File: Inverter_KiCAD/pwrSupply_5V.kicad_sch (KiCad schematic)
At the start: 2 parts, among them U11 17791063215

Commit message: add break
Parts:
- R21: footprint (none) -> Resistor_SMD:R_0603_1608Metric_Pad0.98x0.95mm_HandSolder
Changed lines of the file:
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@@
       (effects (font (size 1.27 1.27)) (justify left))
     )
-    (property "Footprint" "" (at 64.77 34.29 0)
+    (property "Footprint" "Resistor_SMD:R_0603_1608Metric_Pad0.98x0.95mm_HandSolder" (at 64.77 34.29 0)
       (effects (font (size 1.27 1.27)) hide)
     )

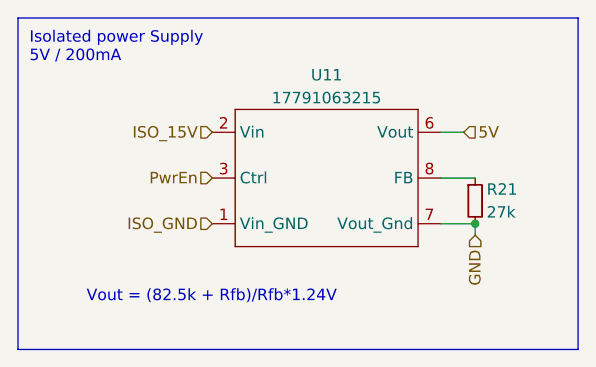
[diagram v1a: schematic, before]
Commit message: clear schematic errors
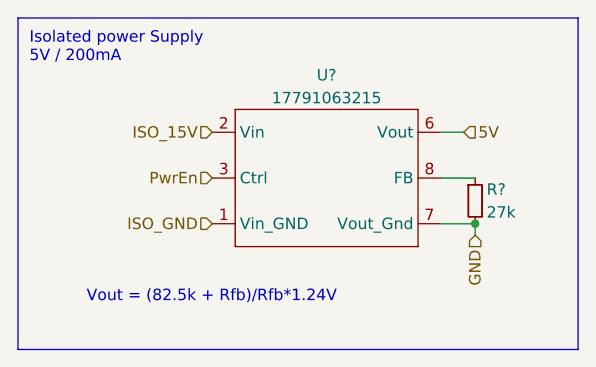
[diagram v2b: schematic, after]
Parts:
- renumbered R21 to R?, U11 to U?
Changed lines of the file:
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@@
   (symbol (lib_id "Custom:17791063215") (at 48.26 31.75 0) (unit 1)
     (in_bom yes) (on_board yes) (dnp no) (fields_autoplaced)
-    (property "Reference" "U11" (at 48.26 20.32 0)
+    (property "Reference" "U?" (at 48.26 20.32 0)
       (effects (font (size 1.27 1.27)))
     )
@@
       (project "Inverter_KiCAD"
         (path "/5e6c1e3f-0815-454a-8acb-8e3e2d064875/68381f6c-5b48-4aca-8792-bde0d1e54d5e"
-          (reference "U11") (unit 1)
+          (reference "U?") (unit 1)
         )
         (path "/5e6c1e3f-0815-454a-8acb-8e3e2d064875/57f5e783-d2a3-41bb-a15a-37a099f233e7"
-          (reference "U11") (unit 1)
+          (reference "U701") (unit 1)
         )
       )
@@
   (symbol (lib_id "Device:R_Small") (at 64.77 34.29 0) (unit 1)
     (in_bom yes) (on_board yes) (dnp no)
-    (property "Reference" "R21" (at 66.04 33.02 0)
+    (property "Reference" "R?" (at 66.04 33.02 0)
       (effects (font (size 1.27 1.27)) (justify left))
     )
@@
       (project "Inverter_KiCAD"
         (path "/5e6c1e3f-0815-454a-8acb-8e3e2d064875/68381f6c-5b48-4aca-8792-bde0d1e54d5e"
-          (reference "R21") (unit 1)
+          (reference "R?") (unit 1)
         )
         (path "/5e6c1e3f-0815-454a-8acb-8e3e2d064875/57f5e783-d2a3-41bb-a15a-37a099f233e7"
-          (reference "R21") (unit 1)
+          (reference "R701") (unit 1)
         )
       )

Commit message: end of sch, start pcb
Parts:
- R?: footprint Resistor_SMD:R_0603_1608Metric_Pad0.98x0.95mm_HandSolder -> Resistor_SMD:R_0402_1005Metric_Pad0.72x0.64mm_HandSolder
- U?: footprint (none) -> Custom:17791063215
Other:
- company: (none) -> ENSEA
- title: (none) -> AAP Inverter
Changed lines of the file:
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@@
 (kicad_sch (version 20230121) (generator eeschema)
   (paper "A4")
+  (title_block
+    (title "AAP Inverter")
+    (date "2023-05-01")
+    (company "ENSEA")
+  )
   (junction (at 64.77 36.83) (diameter 0) (color 0 0 0 0)
   )
@@
       (effects (font (size 1.27 1.27)))
     )
-    (property "Footprint" "" (at 57.15 41.91 0)
+    (property "Footprint" "Custom:17791063215" (at 57.15 41.91 0)
       (effects (font (size 1.27 1.27)) hide)
     )
@@
       (effects (font (size 1.27 1.27)) (justify left))
     )
-    (property "Footprint" "Resistor_SMD:R_0603_1608Metric_Pad0.98x0.95mm_HandSolder" (at 64.77 34.29 0)
+    (property "Footprint" "Resistor_SMD:R_0402_1005Metric_Pad0.72x0.64mm_HandSolder" (at 64.77 34.29 0)
       (effects (font (size 1.27 1.27)) hide)
     )

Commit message: update pcb
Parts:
- R?: footprint Resistor_SMD:R_0402_1005Metric_Pad0.72x0.64mm_HandSolder -> Resistor_SMD:R_0402_1005Metric; Fournisseur (none) -> Stock
- U?: Fournisseur (none) -> Wurth; MFR (none) -> 177 910 632 15
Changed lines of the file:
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@@
+      (effects (font (size 1.27 1.27)) hide)
+    )
+    (property "Fournisseur" "Wurth" (at 48.26 31.75 0)
+      (effects (font (size 1.27 1.27)) hide)
+    )
+    (property "MFR" "177 910 632 15" (at 48.26 31.75 0)
       (effects (font (size 1.27 1.27)) hide)
     )
@@
       (effects (font (size 1.27 1.27)) (justify left))
     )
-    (property "Footprint" "Resistor_SMD:R_0402_1005Metric_Pad0.72x0.64mm_HandSolder" (at 64.77 34.29 0)
+    (property "Footprint" "Resistor_SMD:R_0402_1005Metric" (at 64.77 34.29 0)
       (effects (font (size 1.27 1.27)) hide)
     )
@@
       (effects (font (size 1.27 1.27)) hide)
     )
+    (property "Fournisseur" "Stock" (at 64.77 34.29 0)
+      (effects (font (size 1.27 1.27)) hide)
+    )
